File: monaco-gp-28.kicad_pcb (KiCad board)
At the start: 2 copper layers, 124.9 x 48.2 mm, 2 parts

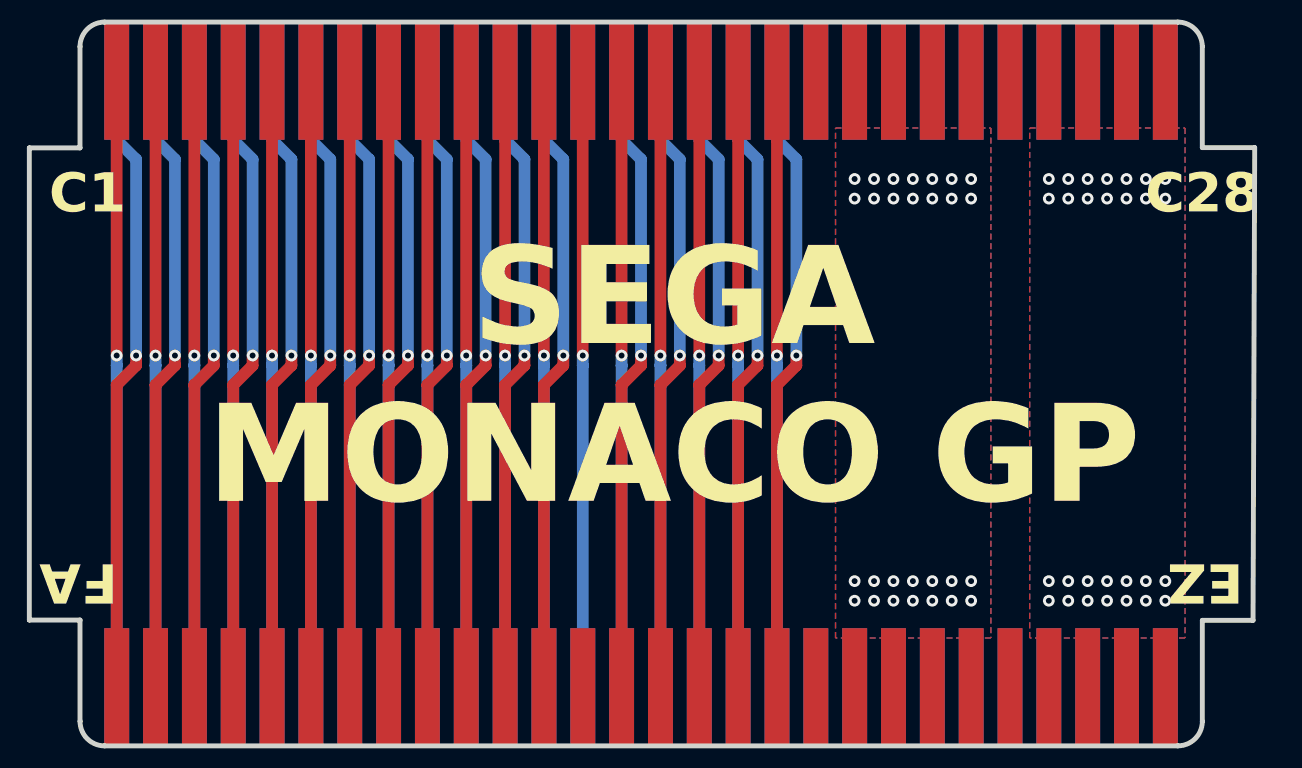
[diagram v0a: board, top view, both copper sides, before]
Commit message: cleanup, add holes, shrink connector size
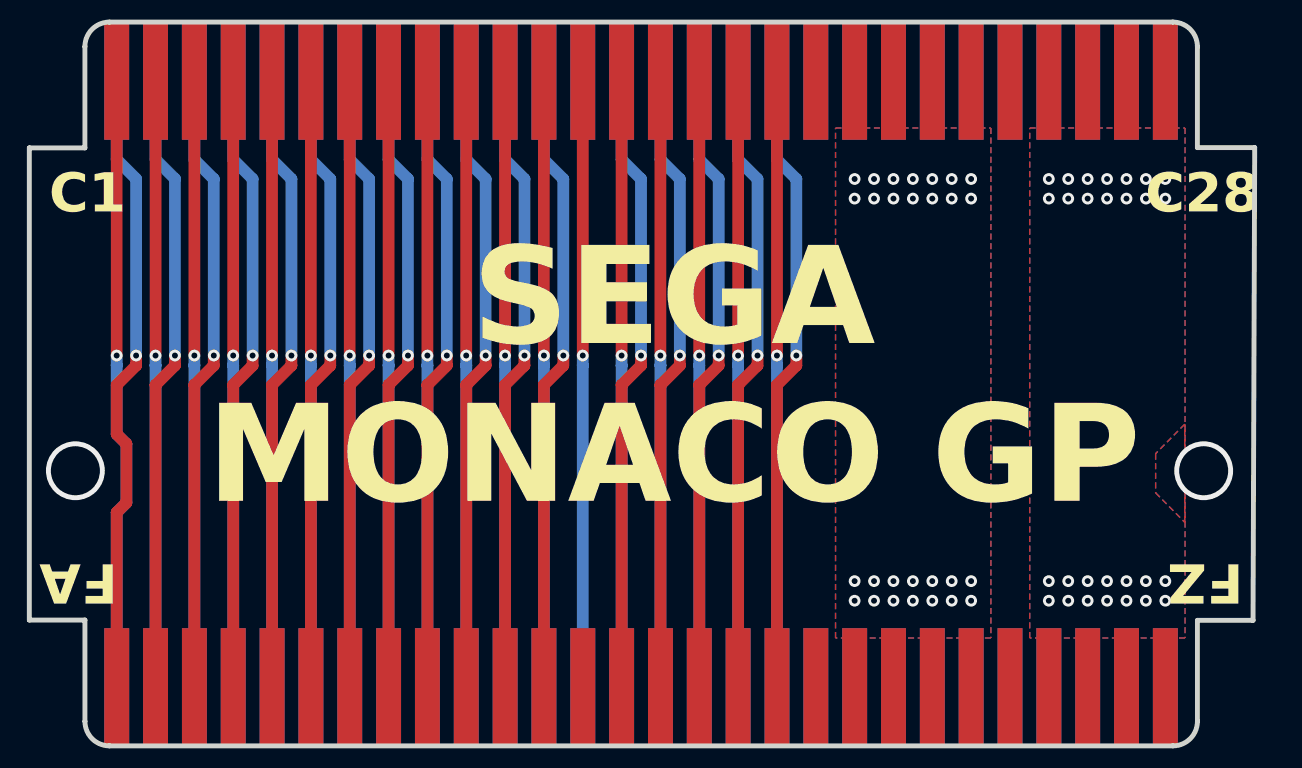
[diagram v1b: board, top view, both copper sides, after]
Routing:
- net /Y45: track 62.6 -> 68.6 mm
- net /Y42: track 62.6 -> 68.6 mm
- net /Y35: track 62.6 -> 68.6 mm
- net /Y46: track 62.6 -> 68.6 mm
- net /Y43: track 62.6 -> 68.6 mm
- net /Y40: track 62.6 -> 68.6 mm
- net /Y39: track 62.6 -> 68.6 mm
- net /Y38: track 62.6 -> 68.6 mm
- net /Y37: track 62.6 -> 68.6 mm
- net /Y36: track 62.6 -> 68.6 mm
- net /Y34: track 62.6 -> 68.6 mm
- net /Y44: track 62.6 -> 68.6 mm
- net /Y33: track 62.6 -> 68.6 mm
- net /Y32: track 62.6 -> 68.6 mm
- net /Y31: track 62.6 -> 68.6 mm
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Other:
- outline, holes or cut-outs redrawn
- board text added: "FZ"
- board text removed: "EZ"
